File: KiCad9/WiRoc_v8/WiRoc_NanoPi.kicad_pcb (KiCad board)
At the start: 6 copper layers, 48 x 68.7 mm, 195 parts, among them J1 Conn_02x05_Odd_Even, J10 Conn_01x09_Socket, J11 Conn_01x05, J2 Conn_01x04, J3 Micro_SD_Card_Det1, J4 Conn_01x09_Socket, J5 Conn_01x04_Socket, J6 HAT_Conn_DBG, J7 Conn_02x05_Odd_Even, J8 Conn_01x06, J9 Conn_Coaxial, Q1 L2N7002WT1G, SW1 SW_SPST, U1 SY6280, U10 SY7069ADC, U11 AllwinnerH3, U12 DDR3, U13 SGM803-RXN3L, U14 KLM8G1GETF-B041, U15 RT8059, U16 RT8059, U17 RT8059, U18 MP2143DJ, U19 ESP32-C5-Board, U2 OLED, U3 AXP209, U4 74HC73, U5 SY6280, U6 BatteryPadM, U7 BatteryPadP, U8 RAK3172-xx-43-SM-xI, U9 PCF8563T, Y1 32.768kHz, Y2 24MHz/CL=12pF

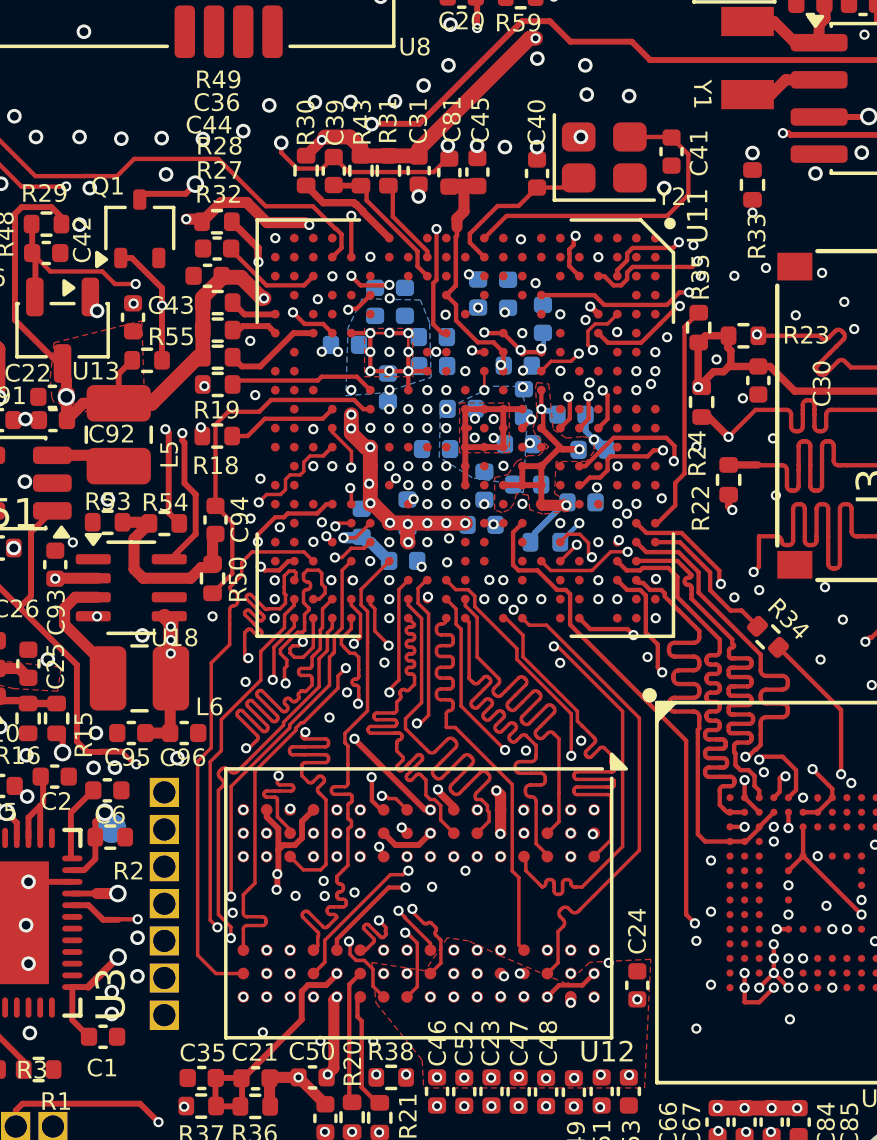
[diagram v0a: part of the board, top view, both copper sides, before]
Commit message: change gnd planes to 0.12 clearance and 0.09 minimum width, move some vias create path inbetween
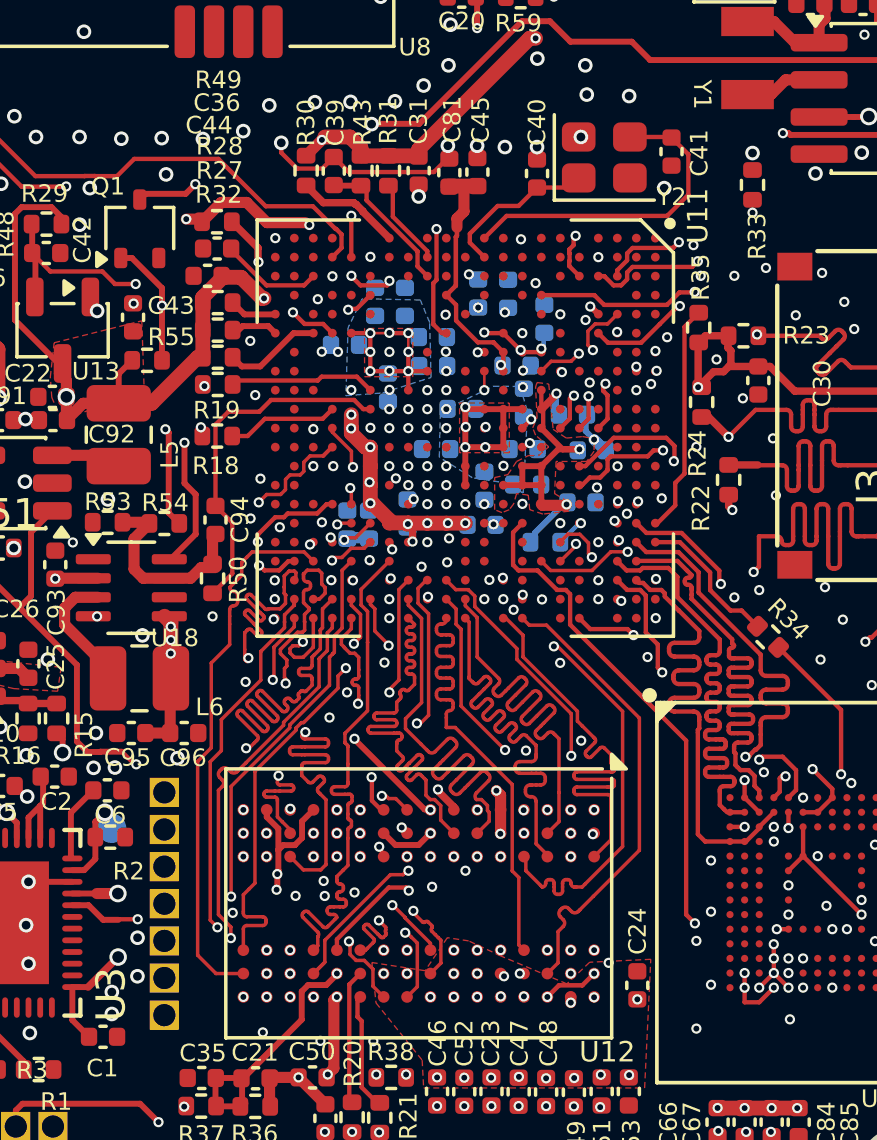
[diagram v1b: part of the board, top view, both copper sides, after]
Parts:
- moved C29 2.28 mm to (72.1, 89.3), turned to 90 degrees
- moved C28 0.26 mm to (72.8, 89.3)
- moved C74 0.23 mm to (78.1, 86.7)
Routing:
- net SVREF: track 34.3 -> 33.1 mm
- net VDD_SYS_3.3V: track 279.0 -> 279.9 mm
- net VDD1V2-SYS: track 40.6 -> 40.1 mm, vias 8 -> 9
- net GND: track 30.4 -> 30.3 mm, vias 401 -> 400
- net VCC-DRAM-1V5: track 28.5 -> 28.4 mm, vias 40 -> 39
